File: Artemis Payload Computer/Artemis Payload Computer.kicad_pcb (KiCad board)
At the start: 2 copper layers, 64.7 x 61 mm, 13 parts, among them J1 Screw_Terminal_01x02, J2 Screw_Terminal_01x02, J601 Connector_Screw_Terminal_01x02, U1 HX711, U2 Teensy3.2, U401 ICM-20948, U501 BMP280, U601 MIC39100-5.0WS, U701 MicroSD_Breakout_Sparkfun

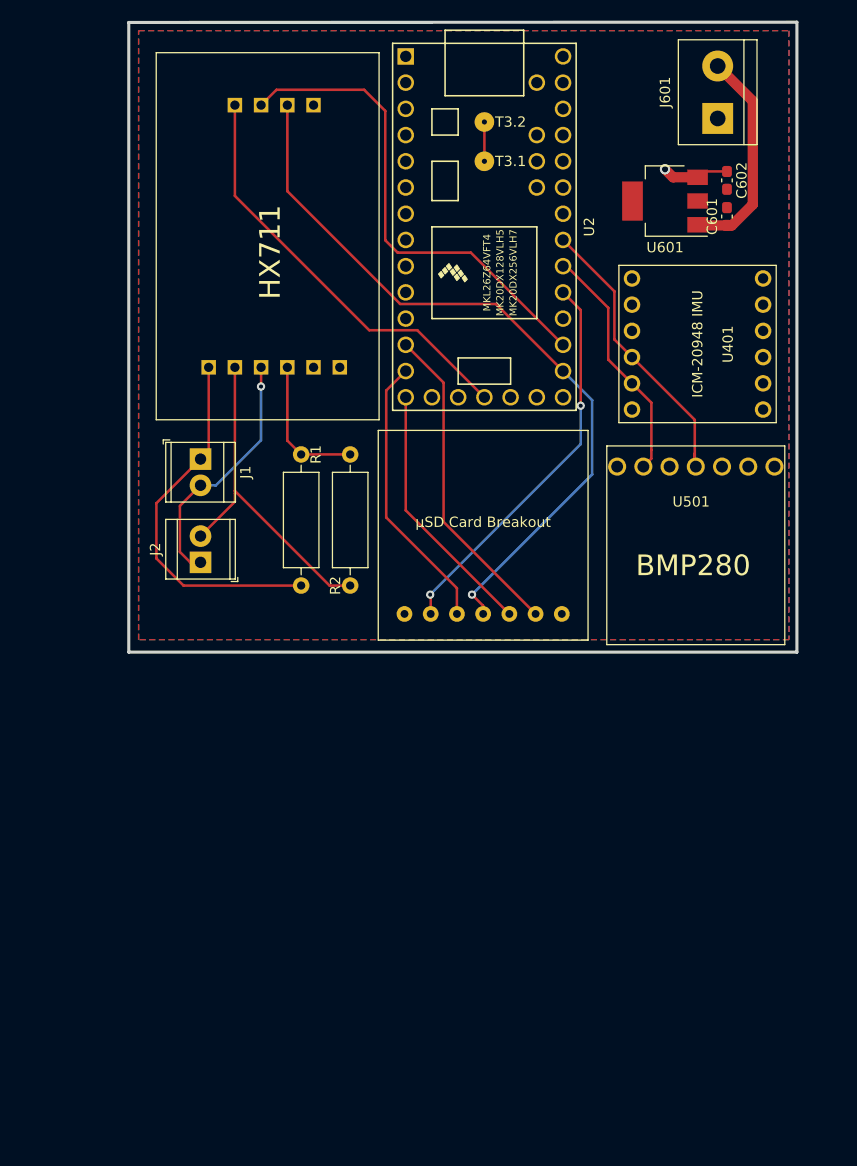
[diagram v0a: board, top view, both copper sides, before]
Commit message: v2 redesign (layout/sizing fixes)
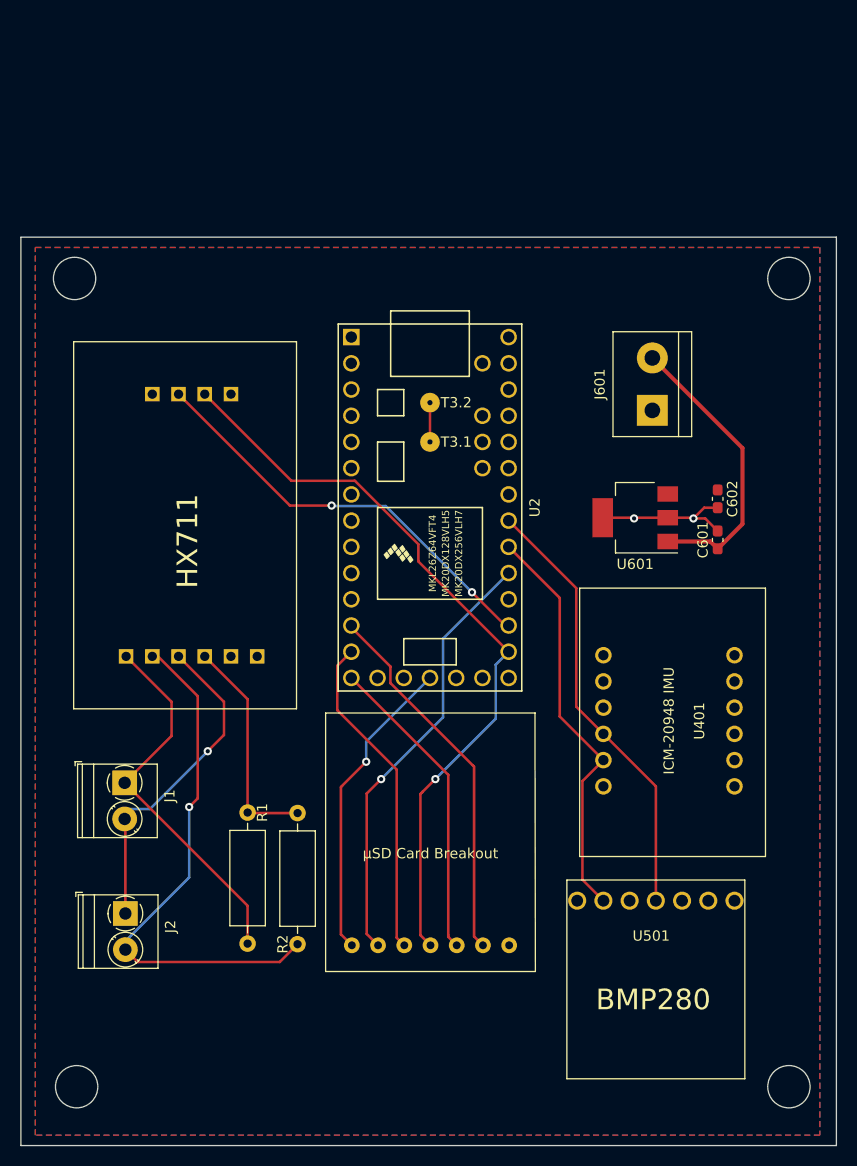
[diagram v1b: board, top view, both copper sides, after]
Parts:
- J1, J2: footprint TerminalBlock_TE-Connectivity:TerminalBlock_TE_282834-2_1x02_P2.54mm_Horizontal -> TerminalBlock_Phoenix:TerminalBlock_Phoenix_PT-1,5-2-3.5-H_1x02_P3.50mm_Horizontal
- moved U501 42.2 mm to (176.7, 115.3)
- moved U401 36.6 mm to (176.7, 91.5)
- moved R2 35.1 mm to (134.4, 119.5)
- moved R1 35.1 mm to (129.6, 106.7)
- moved J2 34.8 mm to (117.7, 116.5), turned to 270 degrees
- moved U701 32.5 mm to (154.9, 119.6)
- moved J1 32.2 mm to (117.7, 103.9)
- moved C601 31.3 mm to (175.1, 80.3)
- moved C602 30.9 mm to (175.1, 76.3)
- moved U601 30.8 mm to (167.1, 78.2)
- moved U1 29.1 mm to (147.0, 100.5)
- moved J601 29.0 mm to (168.8, 67.8)
- moved U2 27.7 mm to (147.2, 77.2)
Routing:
- net Net-(J2-Pad2): track 32.7 -> 51.3 mm, vias 0 -> 1
- net /SDA0: track 23.5 -> 39.8 mm
- net /SCL0: track 27.8 -> 42.7 mm
- net Net-(R1-Pad1): track 13.7 -> 22.1 mm
- net +BATT: track 21.0 -> 28.2 mm
- net Net-(J1-Pad2): track 24.4 -> 31.2 mm
- net +5V: track 6.56 -> 0.00 mm, vias 1 -> 0
- net /DT: track 47.4 -> 41.3 mm, vias 0 -> 2
- net /DI: track 25.1 -> 30.1 mm
- net /CS: track 31.3 -> 36.3 mm
- net /DO: track 27.2 -> 31.7 mm
- net /CD: track 37.9 -> 42.2 mm, vias 2 -> 1
- net GND: track 41.0 -> 44.4 mm, vias 0 -> 3
- net /SCK: track 72.2 -> 73.3 mm
- net Net-(J1-Pad1): track 35.7 -> 36.5 mm
- added copper zone on F.Cu, net +5V
- added copper zone on B.Cu, net GND
- removed copper zone on B.Cu, net +5V
- removed copper zone on F.Cu, net GND
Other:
- board size 64.7 x 61 mm -> 79 x 88 mm
- net class +BATT added: clearance 0.2, trace_width 0.4, via_dia 0.8, via_drill 0.4

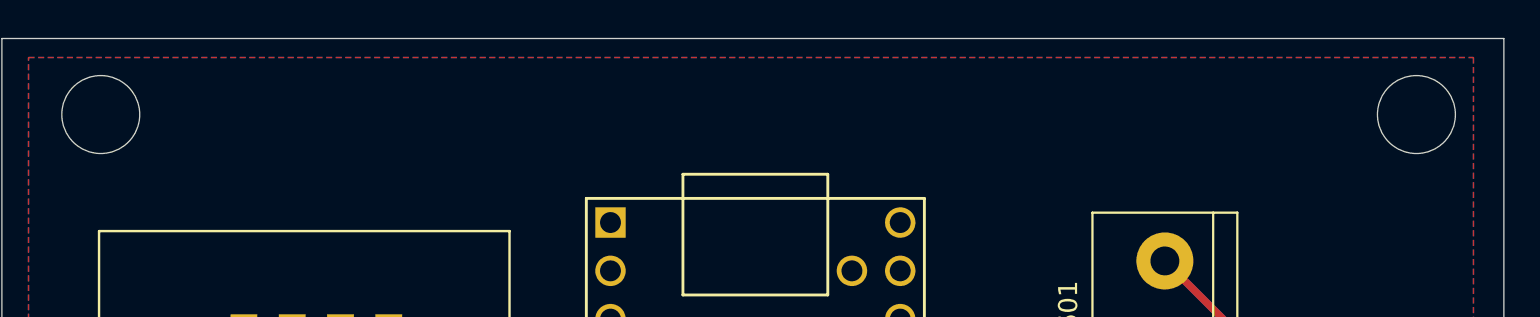
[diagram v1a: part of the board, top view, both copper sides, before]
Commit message: adding text, still need to add logos
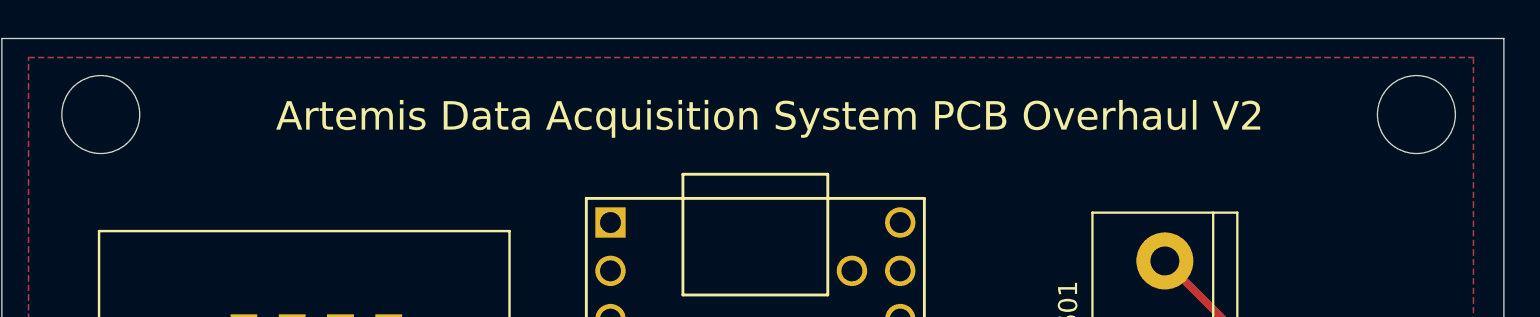
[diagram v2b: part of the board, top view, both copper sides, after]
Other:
- board text added: "Artemis Data Acquisition System PCB Overhaul V2"

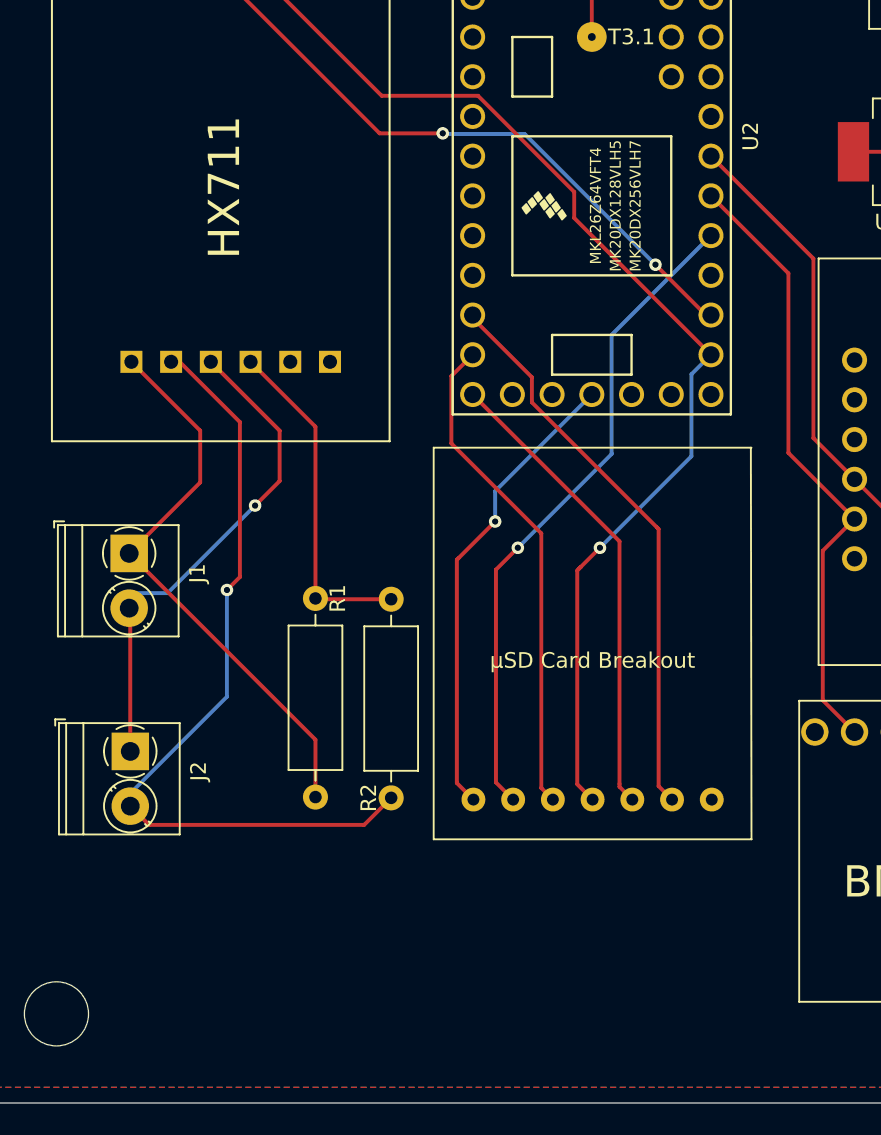
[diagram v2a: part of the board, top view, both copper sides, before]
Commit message: logos added
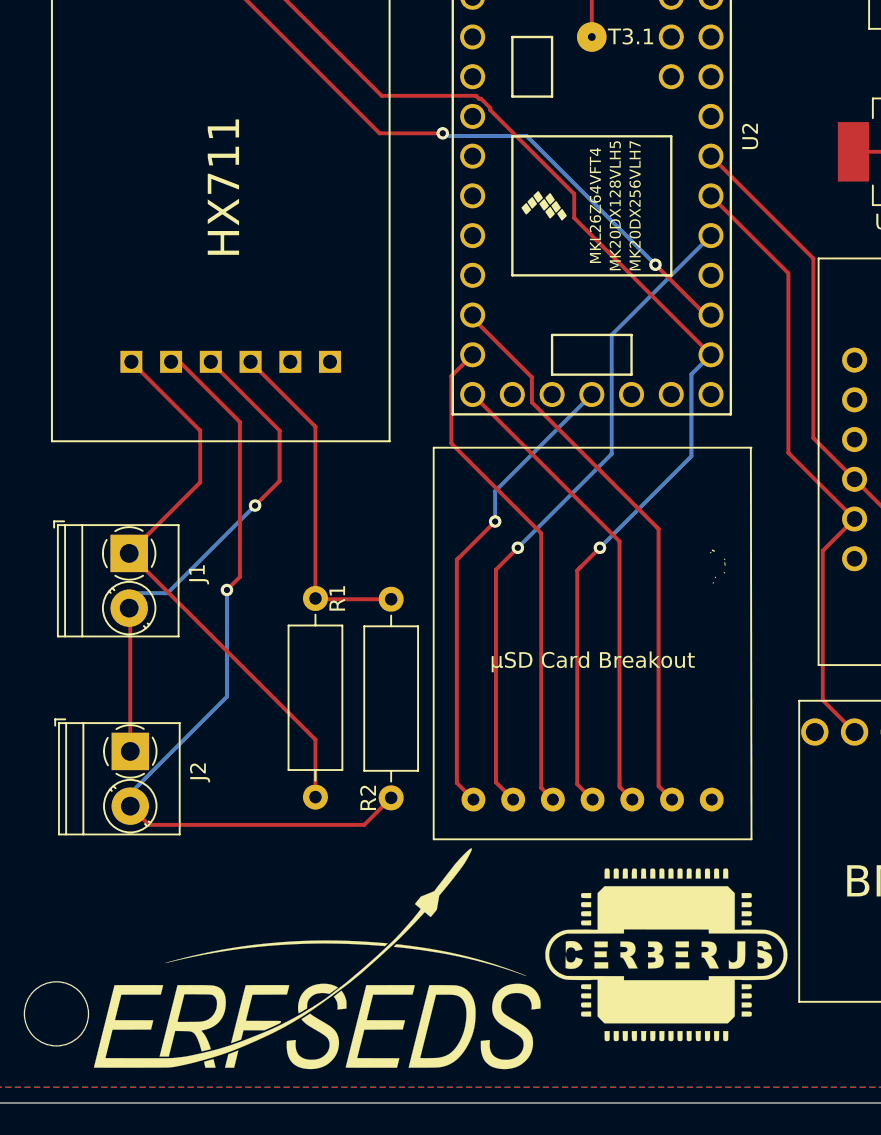
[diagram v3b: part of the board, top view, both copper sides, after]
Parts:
- added G***: LOGO, Artemis Payload Computer:pepe, F.Cu at (152.2, 100.4)
- added G***: LOGO, Artemis Payload Computer:erfseds_logo2, F.Cu at (129.7, 129.7)
- added G***: LOGO, Artemis Payload Computer:cerberus_logo_2, F.Cu at (152.0, 129.5)
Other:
- board text added: "poggers"

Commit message: v2 finalized
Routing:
- net Net-(J2-Pad2): track 51.3 -> 55.0 mm
